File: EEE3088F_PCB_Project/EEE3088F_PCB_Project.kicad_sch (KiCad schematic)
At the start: 18 parts, among them J1 Conn_02x16_Odd_Even, Q1 AO3401A, Q2 AO3401A, Q3 MMBT2222A, Q4 MMBT2222A, U1 TPS62067DSGR, U2 TPS62067DSGR, U3 INA219AIDCNR, U4 DRV8833PWPR, U5 DRV8833PWPR

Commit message: v0.1.2
Lula: Updated ICs with more compact symbols from Component Search Engine
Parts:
- removed Q1, Q2: AO3401A, AO3401A:SOT23, symbol AO3401A:AO3401A
- removed U1, U2: TPS62067DSGR, TPS62067DSGR:SON50P200X200X80-9N, symbol TPS62067DSGR:TPS62067DSGR
- removed U3: INA219AIDCNR, INA219AIDCNR:SOT65P280X145-8N, symbol INA219AIDCNR:INA219AIDCNR
- removed U4, U5: DRV8833PWPR, DRV8833PWPR:IC_DRV8833PWPR, symbol DRV8833PWPR:DRV8833PWPR
- added IC1, IC2: DRV8833PWPR, SOP65P640X120-16N, symbol DRV8833PWPR:DRV8833PWPR
- added IC3, IC4: TPS62067DSGR, SON50P200X200X80-9N, symbol TPS62067DSGR:TPS62067DSGR
- added IC5: INA219AIDCNR, SOP65P280X145-8N, symbol INA219AIDCNR:INA219AIDCNR
- added Q5, Q6: AO3401A, SOT95P280X125-3N, symbol AO3401A:AO3401A
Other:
- moved on the sheet: Q3

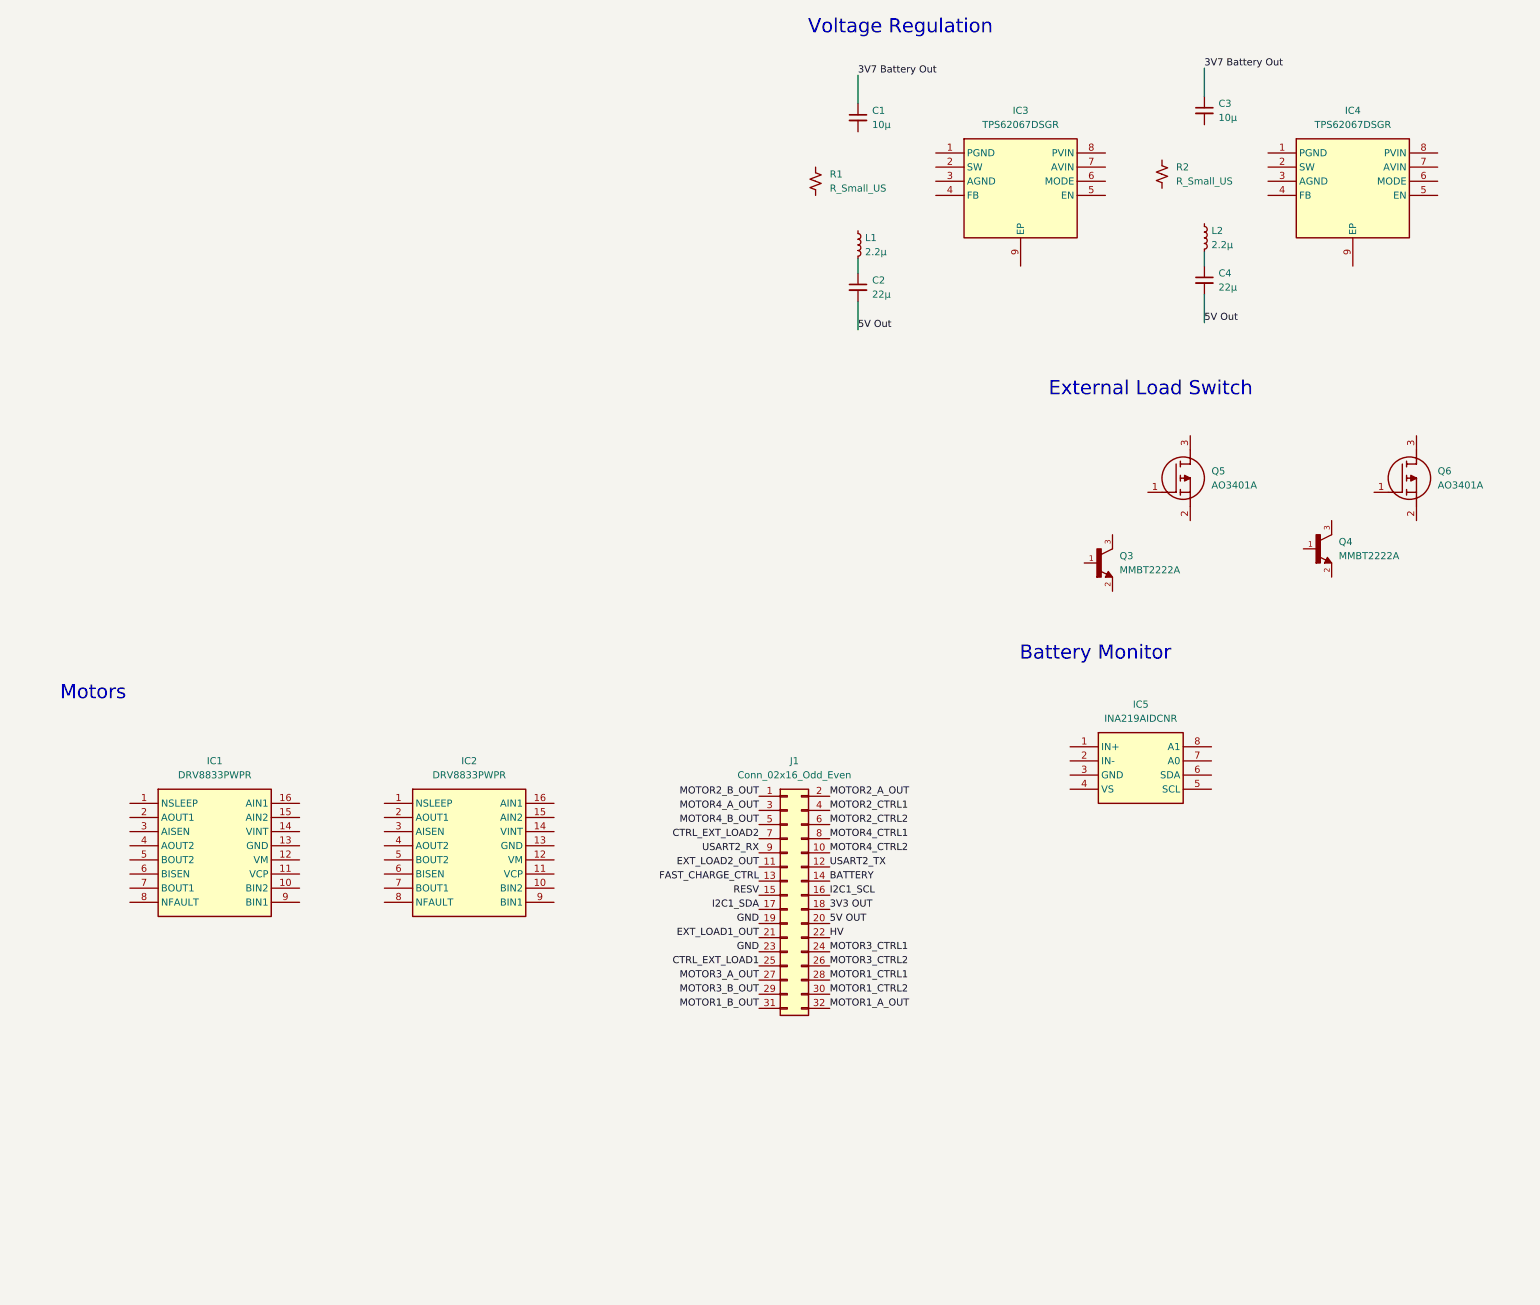
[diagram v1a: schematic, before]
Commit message: v0.2
Lula: rough battery monitor circuit done
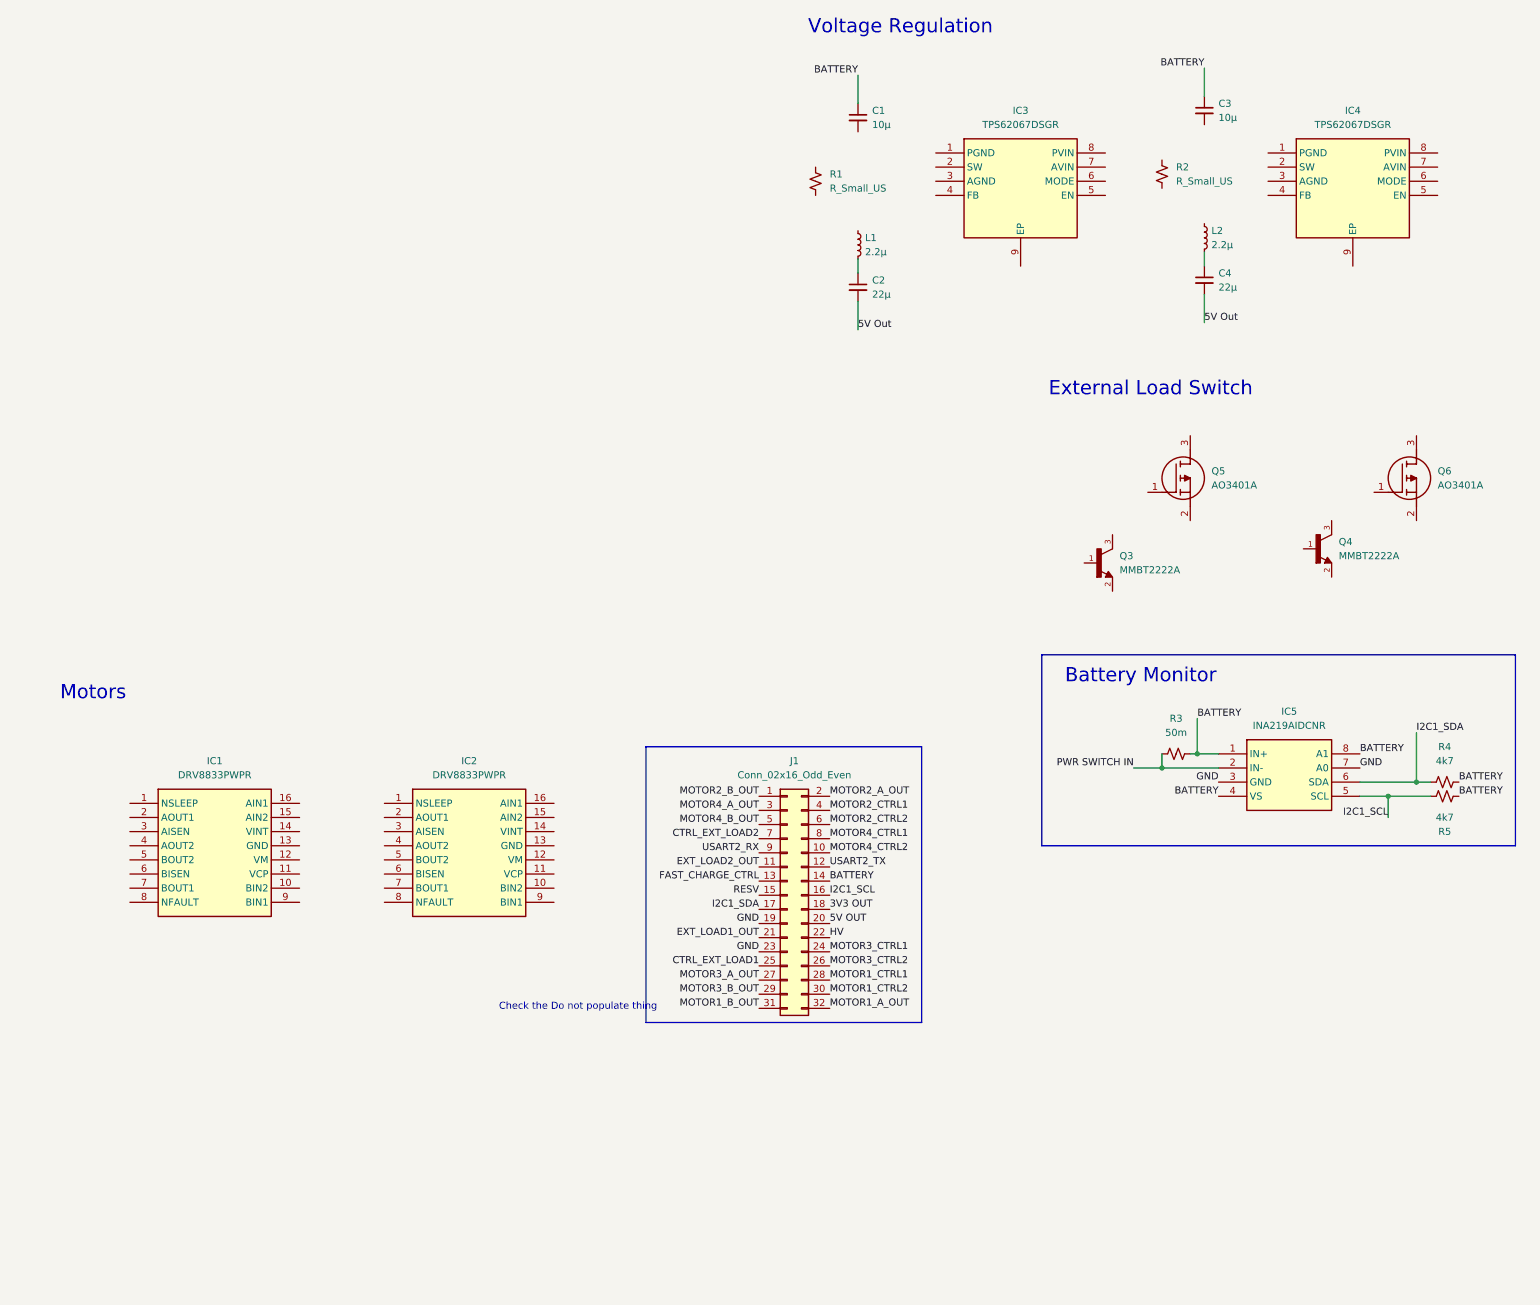
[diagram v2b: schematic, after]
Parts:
- added R3: 50m, symbol Device:R_Small_US
- added R4, R5: 4k7, symbol Device:R_Small_US
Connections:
- net 3V7 Battery Out is gone; now on net BATTERY: C1.1, C3.1
- net BATTERY: now also IC5.1 (IN+), IC5.4 (VS), IC5.8 (A1), R3.2, R4.1, R5.1
- net GND: now also IC5.3 (GND), IC5.7 (A0)
- net I2C1_SCL: now also IC5.5 (SCL), R5.2
- net I2C1_SDA: now also IC5.6 (SDA), R4.2
- net PWR SWITCH IN: now reaches IC5.2 (IN-)
- net PWR SWITCH IN: now also R3.1
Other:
- note added: "Check the Do not populate thing"
- moved on the sheet: IC5

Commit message: v0.2.1
Lula: Making progress with Motor cct
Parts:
- added C5: 10µ, symbol Device:C_Small
- added C6: 2.2µ, symbol Device:C_Small
- added C7: 0.01µ, symbol Device:C_Small
- added R6, R7: 1, symbol Device:R_Small_US
- J1: now not fitted
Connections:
- net 5V OUT: now also IC1.1 (NSLEEP), IC1.12 (VM), C5.1, C7.1
- net GND: now also IC1.13 (GND), C5.2, C6.2, R6.2
- net MOTOR1_A_OUT: now also IC1.2 (AOUT1)
- net MOTOR1_B_OUT: now also IC1.4 (AOUT2)
- net MOTOR1_CTRL1: now also IC1.16 (AIN1)
- net MOTOR1_CTRL2: now also IC1.15 (AIN2)
- net MOTOR2_CTRL1: now also IC1.9 (BIN1)
- net MOTOR2_CTRL2: now also IC1.10 (BIN2)
- net at IC1.11 (VCP): now also C7.2
- net at IC1.14 (VINT): now also C6.1
- net at IC1.3 (AISEN): now also R6.1
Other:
- note added: "Check where resistors necessary. Isen = 200mV / RIsen for 200mA -> 1Ω for 500mA -> 0.4Ω bypass ceramic cap: min 10µF (VM) bypass cap: 2.2µF, 6.3V (VINT) ceramic cap: 0.01-μF, 16-V (minimum) X7R (VCP)"
- note added: "Do not populate: - 2x16 pin connector - battery"
- note removed: "Check the Do not populate thing"
- moved on the sheet: IC1, IC2

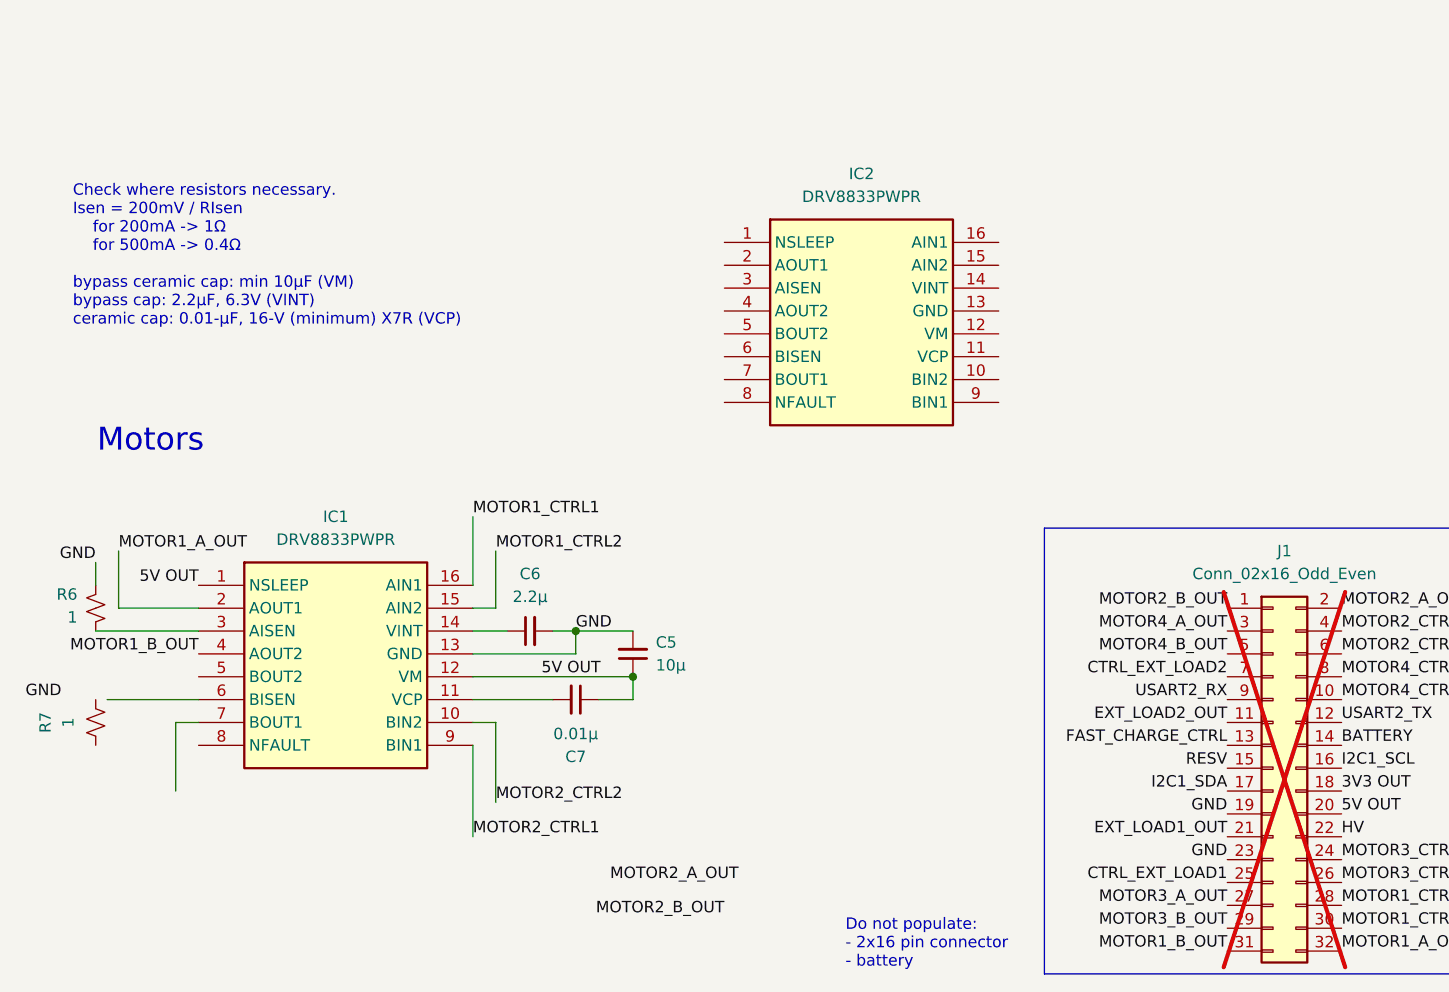
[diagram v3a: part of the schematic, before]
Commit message: v0.3
Lula: rough schematic for motors done
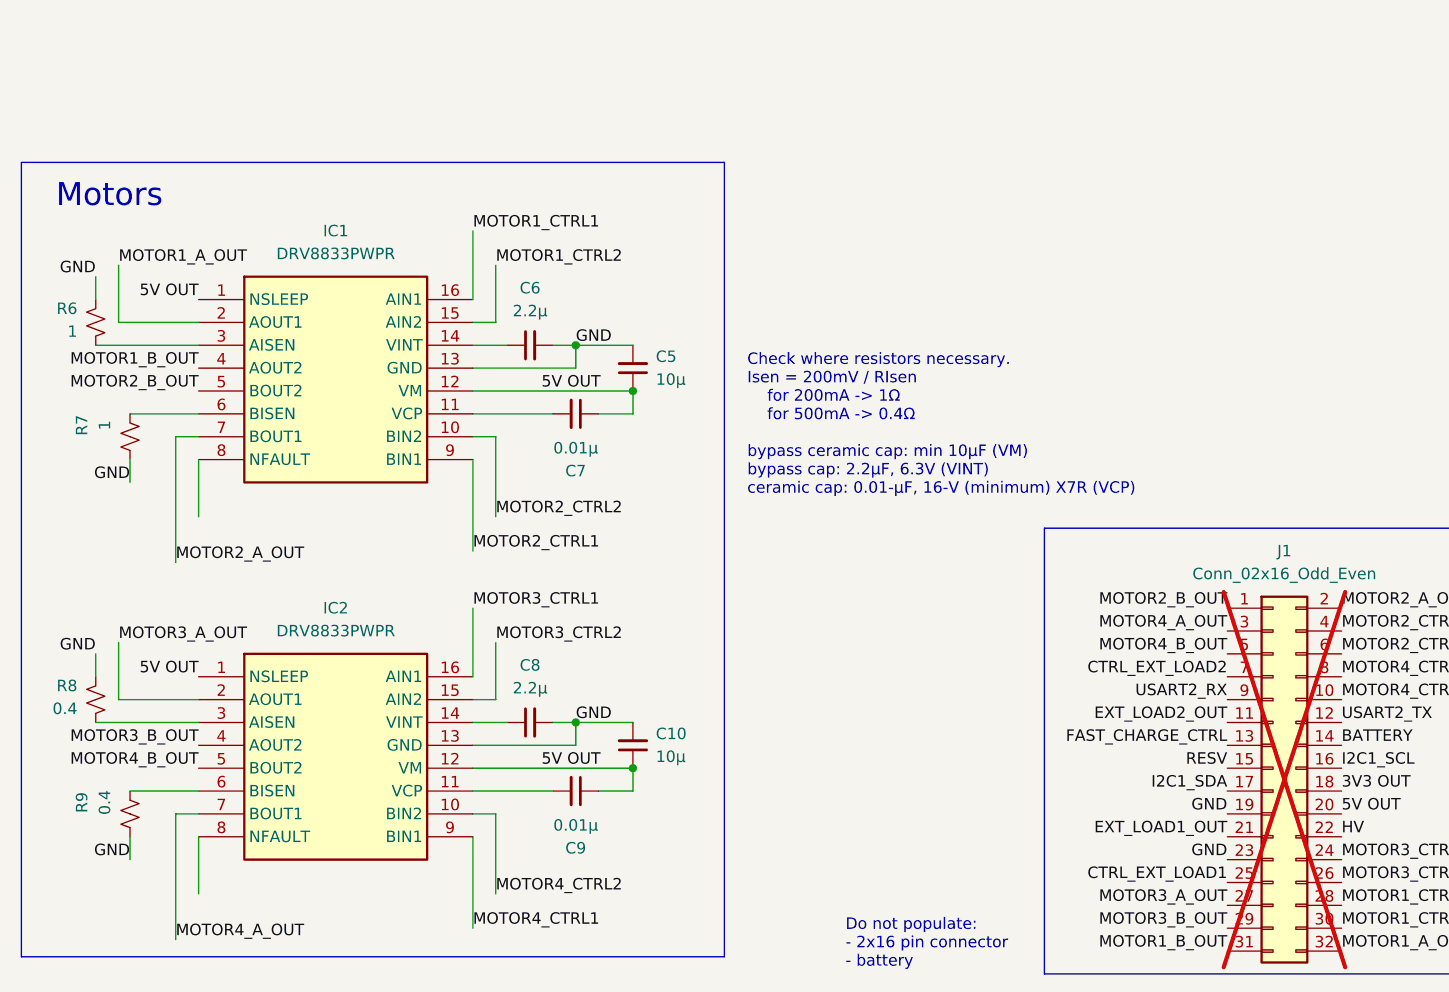
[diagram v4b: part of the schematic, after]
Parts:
- added C10: 10µ, symbol Device:C_Small
- added C8: 2.2µ, symbol Device:C_Small
- added C9: 0.01µ, symbol Device:C_Small
- added R8, R9: 0.4, symbol Device:R_Small_US
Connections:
- net 5V OUT: now also IC2.1 (NSLEEP), IC2.12 (VM), C10.1, C9.1
- net GND: now also IC2.13 (GND), R7.2, C10.2, C8.2, R8.2, R9.2
- net MOTOR2_A_OUT: now also IC1.7 (BOUT1)
- net MOTOR2_B_OUT: now also IC1.5 (BOUT2)
- net MOTOR3_A_OUT: now also IC2.2 (AOUT1)
- net MOTOR3_B_OUT: now also IC2.4 (AOUT2)
- net MOTOR3_CTRL1: now also IC2.16 (AIN1)
- net MOTOR3_CTRL2: now also IC2.15 (AIN2)
- net MOTOR4_A_OUT: now also IC2.7 (BOUT1)
- net MOTOR4_B_OUT: now also IC2.5 (BOUT2)
- net MOTOR4_CTRL1: now also IC2.9 (BIN1)
- net MOTOR4_CTRL2: now also IC2.10 (BIN2)
- net at IC2.11 (VCP): now also C9.2
- net at IC2.14 (VINT): now also C8.1
- net at IC2.3 (AISEN): now also R8.1
- net at IC2.6 (BISEN): now also R9.1
- net at IC1.6 (BISEN): now also R7.1
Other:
- moved on the sheet: C5, C6, C7, IC1, R6, R7
